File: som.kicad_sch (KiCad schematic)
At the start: 34 parts, among them M1 jetson-orin-nx/nano-module, U4 NTS0102GT

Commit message: Renaming Sheets
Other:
- company: Antmicro Ltd -> Dronolab
- title: Jetson Orin Baseboard -> SoM
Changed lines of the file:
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@@
   (paper "A3")
   (title_block
-    (title "Jetson Orin Baseboard")
-    (date "2023-03-03")
-    (rev "1.1.0")
-    (company "Antmicro Ltd")
-    (comment 1 "www.antmicro.com")
+    (title "SoM")
+    (date "2023-07-05")
+    (rev "1.0.0")
+    (company "Dronolab")
+    (comment 1 "dronolab.etsmtl.ca")
   )
   (junction (at 57.15 175.26) (diameter 0) (color 0 0 0 0)

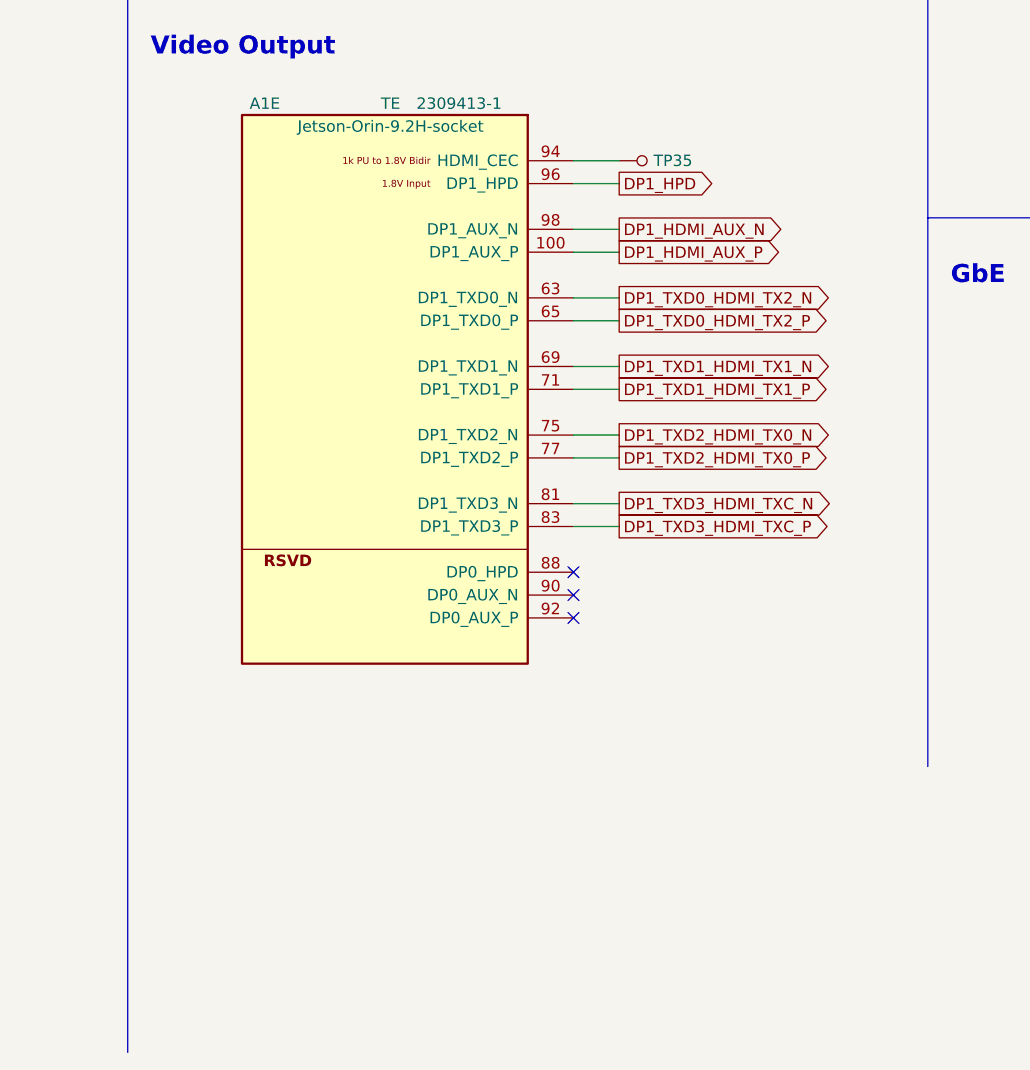
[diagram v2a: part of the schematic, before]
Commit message: Caps and DP to USBC HPD
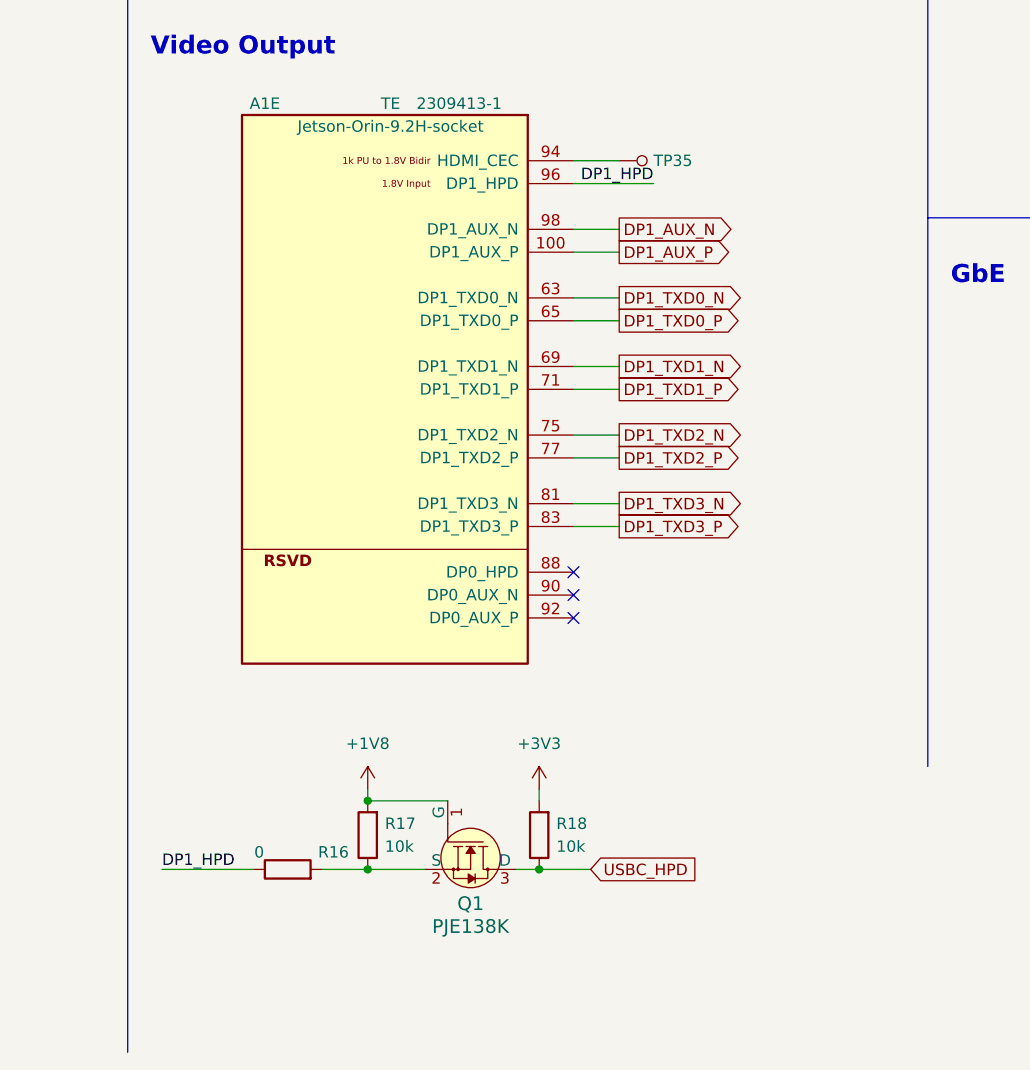
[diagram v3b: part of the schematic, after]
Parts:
- added Q1: PJE138K, jetson-orin-baseboard-footprints:SOT-523, symbol jetson-orin-baseboard:PJE138K
- added R16: 0, symbol Device:R
- added R17, R18: 10k, symbol Device:R
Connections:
- net +1V8: now also Q1.1 (G), R17.2
- net +3V3: now also R18.2
- net DP1_HPD: now also R16.1
- net DP1_HDMI_AUX_N renamed DP1_AUX_N
- net DP1_HDMI_AUX_P renamed DP1_AUX_P
- net DP1_TXD0_HDMI_TX2_N renamed DP1_TXD0_N
- net DP1_TXD0_HDMI_TX2_P renamed DP1_TXD0_P
- net DP1_TXD1_HDMI_TX1_N renamed DP1_TXD1_N
- net DP1_TXD1_HDMI_TX1_P renamed DP1_TXD1_P
- net DP1_TXD2_HDMI_TX0_N renamed DP1_TXD2_N
- net DP1_TXD2_HDMI_TX0_P renamed DP1_TXD2_P
- net DP1_TXD3_HDMI_TXC_N renamed DP1_TXD3_N
- net DP1_TXD3_HDMI_TXC_P renamed DP1_TXD3_P
- new net: Q1.2 (S), R16.2, R17.1
- new net USBC_HPD: Q1.3 (D), R18.1

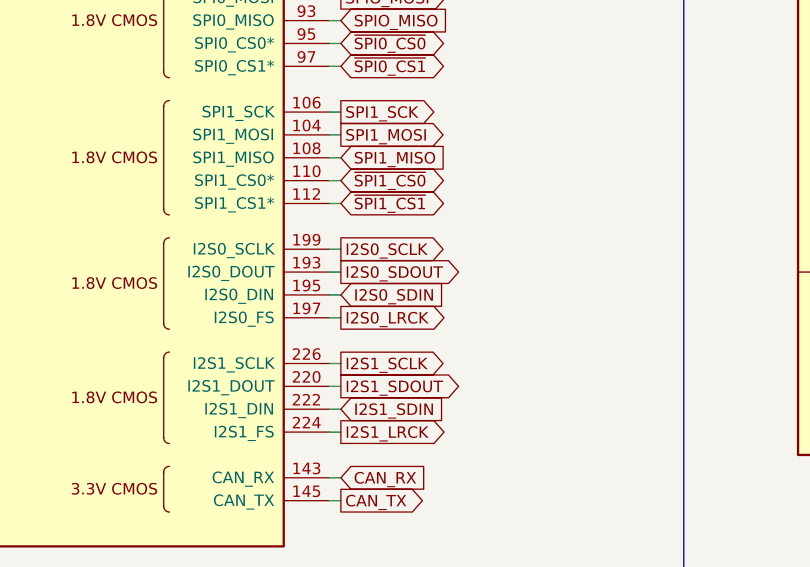
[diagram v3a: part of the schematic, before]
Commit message: Added IMU + MICROPHONES
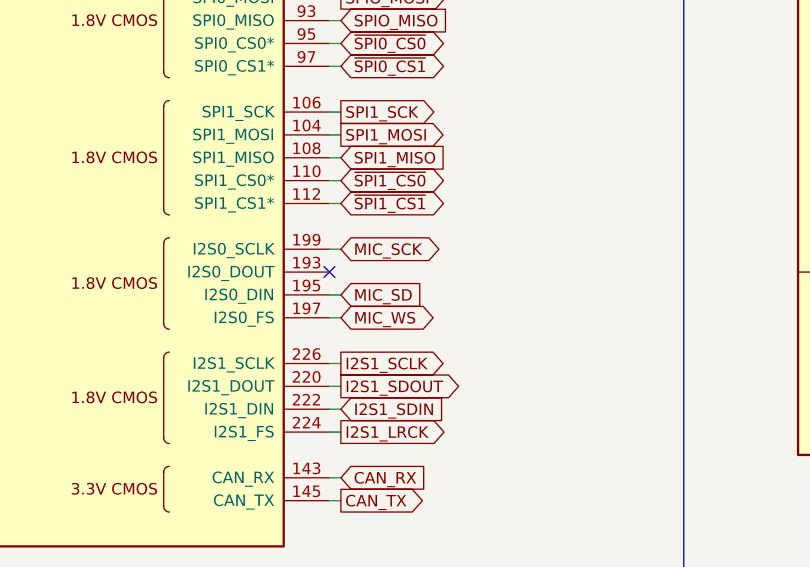
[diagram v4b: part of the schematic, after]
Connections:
- net I2S0_LRCK renamed MIC_WS
- net I2S0_SCLK renamed MIC_SCK
- net I2S0_SDIN renamed MIC_SD
- net I2S0_SDOUT: no longer names the net of A1.193 (I2S0_DOUT)
- no-connect marks 12 -> 13
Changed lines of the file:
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@@
   (title_block
     (title "SoM")
-    (date "2023-07-05")
+    (date "2023-07-09")
     (rev "1.0.0")
     (company "Dronolab")
@@
   (no_connect (at 191.77 43.18))
   (no_connect (at 191.77 45.72))
+  (no_connect (at 189.23 119.38))
   (no_connect (at 109.22 83.82))
   (no_connect (at 278.13 234.95))
@@
     (stroke (width 0) (type default))
   )
-  (wire (pts (xy 190.5 119.38) (xy 189.23 119.38))
-    (stroke (width 0) (type default))
-  )
   (wire (pts (xy 72.39 58.42) (xy 68.58 58.42))
     (stroke (width 0) (type default))
@@
     )
   )
-  (global_label "I2S0_SDIN" (shape input) (at 190.5 121.92 0)
+  (global_label "MIC_SD" (shape input) (at 190.5 121.92 0)
     (effects (font (size 1.27 1.27)) (justify left))
     (property "Intersheetrefs" "${INTERSHEET_REFS}" (at 204.47 121.92 0)
@@
     )
   )
-  (global_label "I2S0_LRCK" (shape output) (at 190.5 124.46 0)
+  (global_label "MIC_WS" (shape bidirectional) (at 190.5 124.46 0)
     (effects (font (size 1.27 1.27)) (justify left))
     (property "Intersheetrefs" "${INTERSHEET_REFS}" (at 204.47 124.46 0)
@@
     )
   )
-  (global_label "I2S0_SCLK" (shape output) (at 190.5 116.84 0)
+  (global_label "MIC_SCK" (shape bidirectional) (at 190.5 116.84 0)
     (effects (font (size 1.27 1.27)) (justify left))
     (property "Intersheetrefs" "${INTERSHEET_REFS}" (at 204.47 116.84 0)
@@
       (effects (font (size 1.27 1.27)) (justify left))
     )
-  )
-  (global_label "I2S0_SDOUT" (shape output) (at 190.5 119.38 0)
-    (effects (font (size 1.27 1.27)) (justify left))
-    (property "Intersheetrefs" "${INTERSHEET_REFS}" (at 204.47 119.38 0)
-      (effects (font (size 1.27 1.27)) (justify left))
-    )

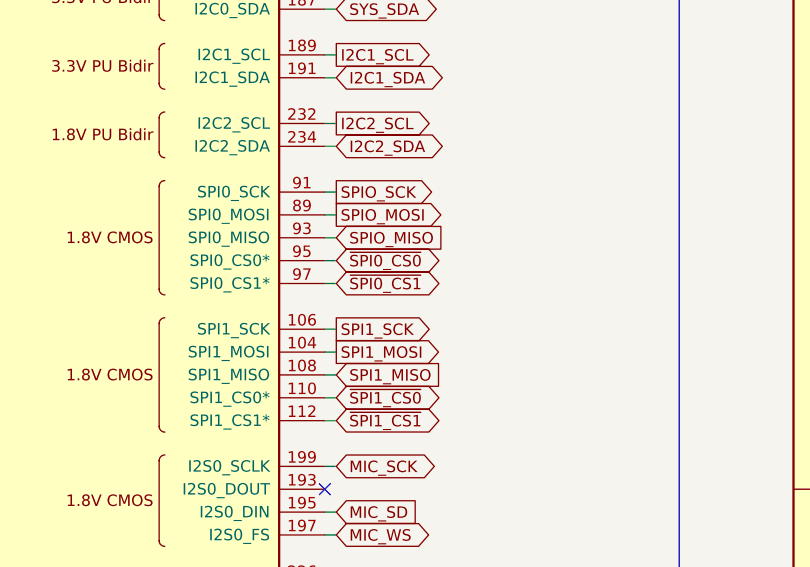
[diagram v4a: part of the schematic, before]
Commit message: Changes to CSI for multiplexing and to peripherals for better PAC connector
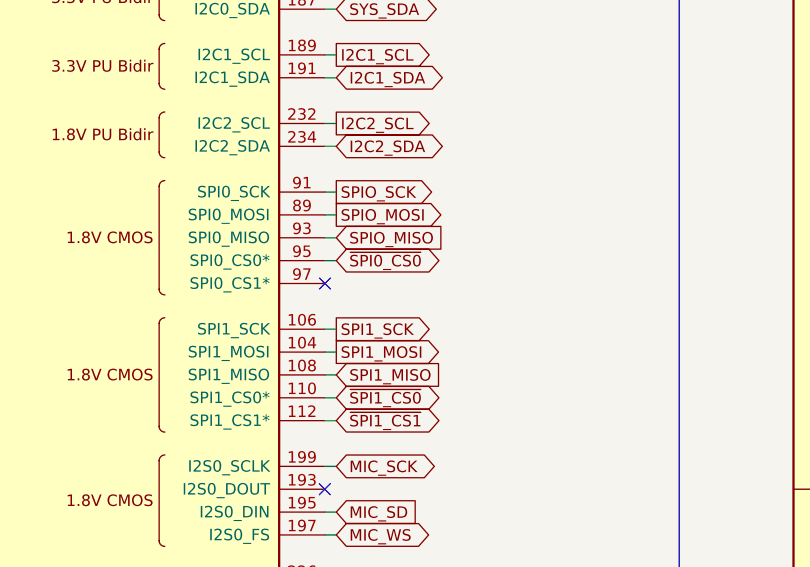
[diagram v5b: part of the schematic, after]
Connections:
- net ~{SPI0_CS1}: no longer names the net of A1.97 (SPI0_CS1*)
- no-connect marks 13 -> 14
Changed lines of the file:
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@@
   (junction (at 110.49 167.64) (diameter 0) (color 0 0 0 0)
   )
+  (no_connect (at 189.23 96.52))
   (no_connect (at 191.77 43.18))
   (no_connect (at 191.77 45.72))
@@
     (stroke (width 0) (type default))
   )
-  (wire (pts (xy 190.5 96.52) (xy 189.23 96.52))
-    (stroke (width 0) (type default))
-  )
   (wire (pts (xy 57.15 144.78) (xy 57.15 142.24))
     (stroke (width 0) (type default))
@@
       (effects (font (size 1.27 1.27)) (justify left))
     )
-  )
-  (global_label "~{SPI0_CS1}" (shape bidirectional) (at 190.5 96.52 0)
-    (effects (font (size 1.27 1.27)) (justify left))
-    (property "Intersheetrefs" "${INTERSHEET_REFS}" (at 204.47 96.52 0)
-      (effects (font (size 1.27 1.27)) (justify left))
-    )

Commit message: Schematic check
Include Pinmux and Schematic Check excels in doc folder and doing a lot of checking and correcting things.
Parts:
- removed R1, R11, R12, R2, R3, R4, R5: R_0R_0402, jetson-orin-baseboard-footprints:0402-res, symbol jetson-orin-baseboard:R_0R_0402
- removed TP4, TP5: TP_SMD_0_75MM, jetson-orin-baseboard-footprints:Testpoint_smd_0_75mm, symbol jetson-orin-baseboard:TP_SMD_0_75MM
- added J14: Conn_01x04, symbol Connector_Generic:Conn_01x04
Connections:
- net +3V3: now also J14.4 (Pin_4)
- net GND: now also J14.3 (Pin_3)
- net GPIO13: now also A1.228 (GPIO13/PWM)
- net CAM1_MCLK: now reaches A1.122 (CAM1_MCLK)
- net CAM0_MCLK: now reaches A1.116 (CAM0_MCLK)
- net CAM0_PWDN: now reaches A1.114 (CAM0_PWDN)
- net CAM1_PWDN: now reaches A1.120 (CAM1_PWDN)
- net USBC1_FLG: now reaches A1.124 (GPIO02)
- net USBC0_FLG: now reaches A1.218 (GPIO12/PWM)
- net CAN_RX: no longer names the net of A1.143 (CAN_RX)
- net CAN_RX: now also J14.2 (Pin_2)
- net CAN_TX: no longer names the net of A1.145 (CAN_TX)
- net CAN_TX: now also J14.1 (Pin_1)
- net CSI1_CLK_N: no longer names the net of A1.9 (CSI1_CLK_N)
- net CSI1_CLK_P: no longer names the net of A1.11 (CSI1_CLK_P)
- net CSI3_CLK_N: no longer names the net of A1.27 (CSI3_CLK_N)
- net CSI3_CLK_P: no longer names the net of A1.29 (CSI3_CLK_P)
- net GPIO01 renamed USBC1_PEN
- net GPIO010 renamed GPIO10
- net GPIO07 renamed GPIO_PAC
- net GPIO11 renamed CAM_MUX_SEL
- net I2C1_SCL: no longer names the net of A1.189 (I2C1_SCL)
- net I2C1_SDA: no longer names the net of A1.191 (I2C1_SDA)
- net I2C2_SCL: no longer names the net of A1.232 (I2C2_SCL)
- net I2C2_SDA: no longer names the net of A1.234 (I2C2_SDA)
- net I2S1_LRCK: no longer names the net of A1.224 (I2S1_FS)
- net I2S1_SCLK: no longer names the net of A1.226 (I2S1_SCLK)
- net I2S1_SDIN: no longer names the net of A1.222 (I2S1_DIN)
- net I2S1_SDOUT: no longer names the net of A1.220 (I2S1_DOUT)
- net MIC_SCK: no longer names the net of A1.199 (I2S0_SCLK)
- net MIC_SD: no longer names the net of A1.195 (I2S0_DIN)
- net MIC_WS: no longer names the net of A1.197 (I2S0_FS)
- net PCIE1_CLKREQ*: no longer names the net of A1.182 (PCIE1_CLKREQ*)
- net PCIE1_CLK_N: no longer names the net of A1.173 (PCIE1_CLK_N)
- net PCIE1_CLK_P: no longer names the net of A1.175 (PCIE1_CLK_P)
- net PCIE1_RST*: no longer names the net of A1.183 (PCIE1_RST*)
- net PCIE1_RX0_N: no longer names the net of A1.167 (PCIE1_RX0_N)
- net PCIE1_RX0_P: no longer names the net of A1.169 (PCIE1_RX0_P)
- net PCIE1_TX0_N: no longer names the net of A1.172 (PCIE1_TX0_N)
- net PCIE1_TX0_P: no longer names the net of A1.174 (PCIE1_TX0_P)
- net PCIE2_CLKREQ*: no longer names the net of A1.221 (PCIE2_CLKREQ*)
- net PCIE2_CLK_N: no longer names the net of A1.52 (PCIE2_CLK_N)
- net PCIE2_CLK_P: no longer names the net of A1.54 (PCIE2_CLK_P)
- net PCIE2_RST*: no longer names the net of A1.219 (PCIE2_RST*)
- net PCIE2_RX0_N: no longer names the net of A1.40 (PCIE2_RX0_N)
- net PCIE2_RX0_P: no longer names the net of A1.42 (PCIE2_RX0_P)
- net PCIE2_RX1_N: no longer names the net of A1.58 (PCIE2_RX1_N/PCIE3_RX0_N)
- net PCIE2_RX1_P: no longer names the net of A1.60 (PCIE2_RX1_P/PCIE3_RX0_P)
- net PCIE2_TX0_N: no longer names the net of A1.46 (PCIE2_TX0_N)
- net PCIE2_TX0_P: no longer names the net of A1.48 (PCIE2_TX0_P)
- net PCIE2_TX1_N: no longer names the net of A1.64 (PCIE2_TX1_N/PCIE3_TX0_N)
- net PCIE2_TX1_P: no longer names the net of A1.66 (PCIE2_TX1_P/PCIE3_TX0_P)
- net PCIE3_CLKREQ*: no longer names the net of A1.225 (PCIE3_CLKREQ*)
- net PCIE3_CLK_N: no longer names the net of A1.227 (PCIE3_CLK_N)
- net PCIE3_CLK_P: no longer names the net of A1.229 (PCIE3_CLK_P)
- net PCIE3_RST*: no longer names the net of A1.223 (PCIE3_RST*)
- net SPI1_MISO: no longer names the net of A1.108 (SPI1_MISO)
- net SPI1_MOSI: no longer names the net of A1.104 (SPI1_MOSI)
- net SPI1_SCK: no longer names the net of A1.106 (SPI1_SCK)
- net UART0_CTS: no longer names the net of A1.105 (UART0_CTS*)
- net UART0_RTS: no longer names the net of A1.103 (UART0_RTS*)
- net UART0_RXD: no longer names the net of A1.101 (UART0_RXD)
- net UART0_TXD: no longer names the net of A1.99 (UART0_TXD)
- net USB1_D_N: no longer names the net of A1.115 (USB1_D_N)
- net USB1_D_P: no longer names the net of A1.117 (USB1_D_P)
- net ~{SPI1_CS0}: no longer names the net of A1.110 (SPI1_CS0*)
- net ~{SPI1_CS1}: no longer names the net of A1.112 (SPI1_CS1*)
- no-connect marks 14 -> 64
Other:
- moved on the sheet: TP35

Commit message: Small changes
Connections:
- net GPIO13: no longer names the net of A1.228 (GPIO13/PWM)
- no-connect marks 64 -> 65
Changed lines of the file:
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@@
   (no_connect (at 367.03 111.76))
   (no_connect (at 189.23 134.62))
+  (no_connect (at 68.58 58.42))
   (no_connect (at 367.03 129.54))
   (no_connect (at 189.23 236.22))
@@
     (stroke (width 0) (type default))
   )
-  (wire (pts (xy 68.58 58.42) (xy 95.25 58.42))
-    (stroke (width 0) (type default))
-  )
   (wire (pts (xy 367.03 66.04) (xy 377.19 66.04))
     (stroke (width 0) (type default))
@@
     )
   )
-  (global_label "GPIO_PAC" (shape bidirectional) (at 95.25 45.72 0)
+  (global_label "GPIO_PAC" (shape input) (at 95.25 45.72 0)
     (effects (font (size 1.27 1.27)) (justify left))
     (property "Intersheetrefs" "${INTERSHEET_REFS}" (at 109.855 45.72 0)
@@
     )
   )
-  (global_label "GPIO13" (shape bidirectional) (at 95.25 58.42 0)
-    (effects (font (size 1.27 1.27)) (justify left))
-    (property "Intersheetrefs" "${INTERSHEET_REFS}" (at 109.855 58.42 0)
-      (effects (font (size 1.27 1.27)) (justify left))
-    )
-  )

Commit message: Schematic Done
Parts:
- added TP1: TestPoint, symbol Connector:TestPoint
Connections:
- net DP1_HPD: now also TP1.1
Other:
- moved on the sheet: A1E, BAT1, C1, C2, C38, C39, D34, D55, FB1, J14, R294, R80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
